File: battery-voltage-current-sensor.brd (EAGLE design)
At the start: 100 x 100 mm, 66 parts, among them IC1 ACS758LCB-050B-PFF-T, IC3 ADS1115IDGST, T1 C8545, T2 C8545, T3 C8545, X1 MKDSN1,5/2-5,08

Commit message: ready to manufacture, ordered
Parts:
- moved H1 0.60 mm to (17.4, 6.00)
- moved H2 0.60 mm to (17.4, 94.0)
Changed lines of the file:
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@@
 <layer number="25" name="tNames" color="7" fill="1" visible="yes" active="yes"/>
 <layer number="26" name="bNames" color="7" fill="1" visible="yes" active="yes"/>
-<layer number="27" name="tValues" color="7" fill="1" visible="no" active="yes"/>
-<layer number="28" name="bValues" color="7" fill="1" visible="no" active="yes"/>
+<layer number="27" name="tValues" color="7" fill="1" visible="yes" active="yes"/>
+<layer number="28" name="bValues" color="7" fill="1" visible="yes" active="yes"/>
 <layer number="29" name="tStop" color="7" fill="3" visible="no" active="yes"/>
 <layer number="30" name="bStop" color="7" fill="6" visible="no" active="yes"/>
@@
 <layer number="42" name="bRestrict" color="1" fill="10" visible="yes" active="yes"/>
 <layer number="43" name="vRestrict" color="2" fill="10" visible="no" active="yes"/>
-<layer number="44" name="Drills" color="7" fill="1" visible="no" active="yes"/>
-<layer number="45" name="Holes" color="7" fill="1" visible="no" active="yes"/>
+<layer number="44" name="Drills" color="7" fill="1" visible="yes" active="yes"/>
+<layer number="45" name="Holes" color="7" fill="1" visible="yes" active="yes"/>
 <layer number="46" name="Milling" color="3" fill="1" visible="no" active="yes"/>
 <layer number="47" name="Measures" color="7" fill="1" visible="no" active="yes"/>
@@
 <attribute name="VALUE" x="36.935" y="38.49" size="1.27" layer="27" align="center"/>
 </element>
-<element name="H1" library="holes" library_urn="urn:adsk.eagle:library:237" package="5,5-PAD-SQUARE" package3d_urn="urn:adsk.eagle:package:14299/1" value="MOUNT-PAD-SQUARE5.5" x="17.4" y="6.6" smashed="yes">
-<attribute name="POPULARITY" value="0" x="17.4" y="6.6" size="1.778" layer="27" display="off"/>
-</element>
-<element name="H2" library="holes" library_urn="urn:adsk.eagle:library:237" package="5,5-PAD-SQUARE" package3d_urn="urn:adsk.eagle:package:14299/1" value="MOUNT-PAD-SQUARE5.5" x="17.4" y="93.4" smashed="yes">
-<attribute name="POPULARITY" value="0" x="17.4" y="93.4" size="1.778" layer="27" display="off"/>
+<element name="H1" library="holes" library_urn="urn:adsk.eagle:library:237" package="5,5-PAD-SQUARE" package3d_urn="urn:adsk.eagle:package:14299/1" value="MOUNT-PAD-SQUARE5.5" x="17.4" y="6" smashed="yes">
+<attribute name="POPULARITY" value="0" x="17.4" y="6" size="1.778" layer="27" display="off"/>
+</element>
+<element name="H2" library="holes" library_urn="urn:adsk.eagle:library:237" package="5,5-PAD-SQUARE" package3d_urn="urn:adsk.eagle:package:14299/1" value="MOUNT-PAD-SQUARE5.5" x="17.4" y="94" smashed="yes">
+<attribute name="POPULARITY" value="0" x="17.4" y="94" size="1.778" layer="27" display="off"/>
 </element>
 <element name="H3" library="holes" library_urn="urn:adsk.eagle:library:237" package="5,5-PAD-SQUARE" package3d_urn="urn:adsk.eagle:package:14299/1" value="MOUNT-PAD-SQUARE5.5" x="50" y="94" smashed="yes">
@@
 <contactref element="R12" pad="1"/>
 <polygon width="0" layer="1" thermals="no">
-<vertex x="66" y="100.5"/>
+<vertex x="66.6" y="100.5"/>
 <vertex x="100.4" y="100.5"/>
-<vertex x="100.4" y="-1.1"/>
-<vertex x="66" y="-1.1"/>
+<vertex x="100.4" y="-1"/>
+<vertex x="66.6" y="-1"/>
 </polygon>
 <polygon width="0" layer="16" thermals="no">
-<vertex x="66" y="100.1"/>
+<vertex x="66.6" y="100.1"/>
 <vertex x="100.1" y="100.1"/>
 <vertex x="100.1" y="-0.1"/>
-<vertex x="66" y="-0.1"/>
+<vertex x="66.6" y="-0.1"/>
 </polygon>
 <wire x1="44.45" y1="65.2" x2="45.65" y2="64" width="0.254" layer="1"/>

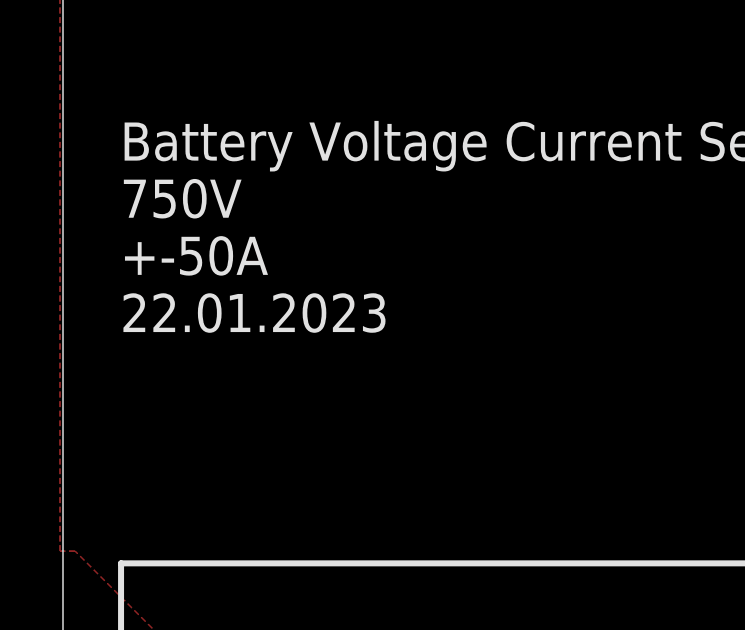
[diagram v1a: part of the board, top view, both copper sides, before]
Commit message: voltage measurement resistors changed to 100k
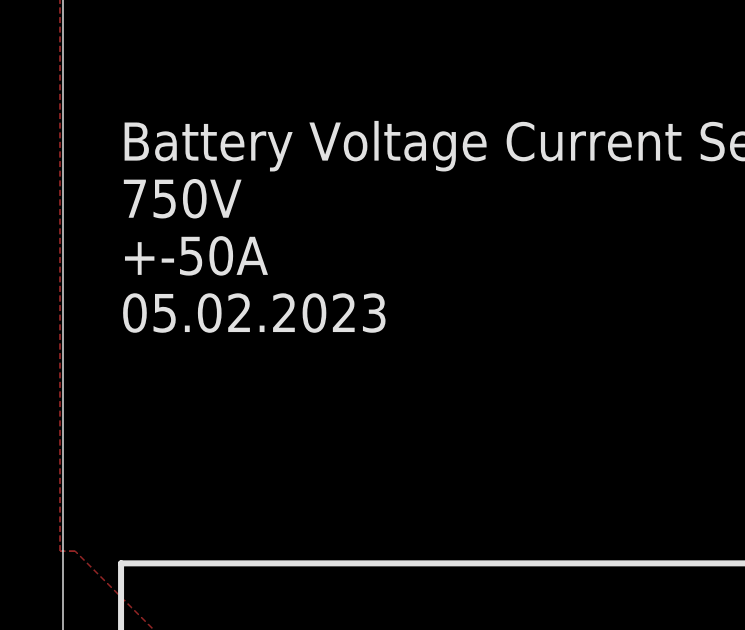
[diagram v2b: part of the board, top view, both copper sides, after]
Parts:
- R15, R16, R17, R18, R19, R20, R21, R22, R23, R4: value C17902 -> C17900
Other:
- board text added: "Battery Voltage Current Sensor 750V +-50A 05.02.2023"
- board text removed: "Battery Voltage Current Sensor 750V +-50A 22.01.2023"
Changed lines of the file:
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@@
 750V
 +-50A
-22.01.2023</text>
+05.02.2023</text>
 <text x="31.6" y="97" size="1.778" layer="25">Battery</text>
 <text x="30.4" y="2.8" size="1.778" layer="25">Output</text>
@@
 <attribute name="VALUE" x="81.6" y="91.2" size="1.27" layer="27" align="center"/>
 </element>
-<element name="R4" library="rcl" library_urn="urn:adsk.eagle:library:334" package="R1206" package3d_urn="urn:adsk.eagle:package:23540/2" value="C17902" x="44.4" y="67.7" smashed="yes" rot="R180"/>
-<element name="R15" library="rcl" library_urn="urn:adsk.eagle:library:334" package="R1206" package3d_urn="urn:adsk.eagle:package:23540/2" value="C17902" x="40.8" y="69.2" smashed="yes" rot="R90"/>
-<element name="R16" library="rcl" library_urn="urn:adsk.eagle:library:334" package="R1206" package3d_urn="urn:adsk.eagle:package:23540/2" value="C17902" x="39.3" y="72.8" smashed="yes" rot="R180"/>
-<element name="R17" library="rcl" library_urn="urn:adsk.eagle:library:334" package="R1206" package3d_urn="urn:adsk.eagle:package:23540/2" value="C17902" x="35.7" y="74.3" smashed="yes" rot="R90"/>
-<element name="R18" library="rcl" library_urn="urn:adsk.eagle:library:334" package="R1206" package3d_urn="urn:adsk.eagle:package:23540/2" value="C17902" x="35.7" y="79.4" smashed="yes" rot="R90"/>
-<element name="R19" library="rcl" library_urn="urn:adsk.eagle:library:334" package="R1206" package3d_urn="urn:adsk.eagle:package:23540/2" value="C17902" x="35.7" y="84.5" smashed="yes" rot="R90"/>
-<element name="R20" library="rcl" library_urn="urn:adsk.eagle:library:334" package="R1206" package3d_urn="urn:adsk.eagle:package:23540/2" value="C17902" x="35.7" y="89.6" smashed="yes" rot="R90"/>
-<element name="R21" library="rcl" library_urn="urn:adsk.eagle:library:334" package="R1206" package3d_urn="urn:adsk.eagle:package:23540/2" value="C17902" x="34.2" y="93.2" smashed="yes" rot="R180"/>
-<element name="R22" library="rcl" library_urn="urn:adsk.eagle:library:334" package="R1206" package3d_urn="urn:adsk.eagle:package:23540/2" value="C17902" x="31.4" y="95.3" smashed="yes" rot="R180"/>
-<element name="R23" library="rcl" library_urn="urn:adsk.eagle:library:334" package="R1206" package3d_urn="urn:adsk.eagle:package:23540/2" value="C17902" x="28.5" y="97.5" smashed="yes" rot="R180"/>
+<element name="R4" library="rcl" library_urn="urn:adsk.eagle:library:334" package="R1206" package3d_urn="urn:adsk.eagle:package:23540/2" value="C17900" x="44.4" y="67.7" smashed="yes" rot="R180"/>
+<element name="R15" library="rcl" library_urn="urn:adsk.eagle:library:334" package="R1206" package3d_urn="urn:adsk.eagle:package:23540/2" value="C17900" x="40.8" y="69.2" smashed="yes" rot="R90"/>
+<element name="R16" library="rcl" library_urn="urn:adsk.eagle:library:334" package="R1206" package3d_urn="urn:adsk.eagle:package:23540/2" value="C17900" x="39.3" y="72.8" smashed="yes" rot="R180"/>
+<element name="R17" library="rcl" library_urn="urn:adsk.eagle:library:334" package="R1206" package3d_urn="urn:adsk.eagle:package:23540/2" value="C17900" x="35.7" y="74.3" smashed="yes" rot="R90"/>
+<element name="R18" library="rcl" library_urn="urn:adsk.eagle:library:334" package="R1206" package3d_urn="urn:adsk.eagle:package:23540/2" value="C17900" x="35.7" y="79.4" smashed="yes" rot="R90"/>
+<element name="R19" library="rcl" library_urn="urn:adsk.eagle:library:334" package="R1206" package3d_urn="urn:adsk.eagle:package:23540/2" value="C17900" x="35.7" y="84.5" smashed="yes" rot="R90"/>
+<element name="R20" library="rcl" library_urn="urn:adsk.eagle:library:334" package="R1206" package3d_urn="urn:adsk.eagle:package:23540/2" value="C17900" x="35.7" y="89.6" smashed="yes" rot="R90"/>
+<element name="R21" library="rcl" library_urn="urn:adsk.eagle:library:334" package="R1206" package3d_urn="urn:adsk.eagle:package:23540/2" value="C17900" x="34.2" y="93.2" smashed="yes" rot="R180"/>
+<element name="R22" library="rcl" library_urn="urn:adsk.eagle:library:334" package="R1206" package3d_urn="urn:adsk.eagle:package:23540/2" value="C17900" x="31.4" y="95.3" smashed="yes" rot="R180"/>
+<element name="R23" library="rcl" library_urn="urn:adsk.eagle:library:334" package="R1206" package3d_urn="urn:adsk.eagle:package:23540/2" value="C17900" x="28.5" y="97.5" smashed="yes" rot="R180"/>
 <element name="R24" library="rcl" library_urn="urn:adsk.eagle:library:334" package="R0805" package3d_urn="urn:adsk.eagle:package:23553/2" value="C17772" x="45.9" y="71.15" smashed="yes" rot="R270"/>
 <element name="C4" library="rcl" library_urn="urn:adsk.eagle:library:334" package="C0805" package3d_urn="urn:adsk.eagle:package:23617/2" value="100nF" x="76.5" y="92.3" smashed="yes" rot="R180">

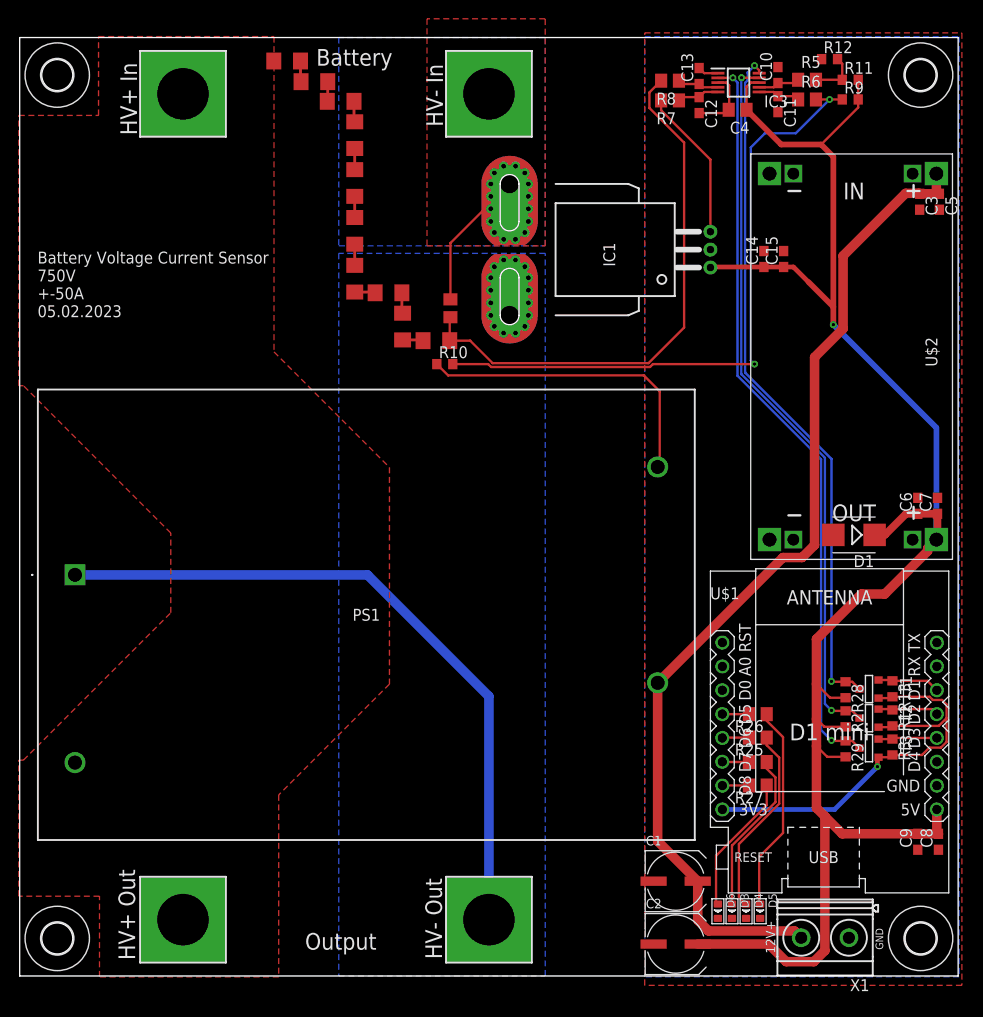
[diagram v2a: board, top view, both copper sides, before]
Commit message: 1000V DCDC position corrected
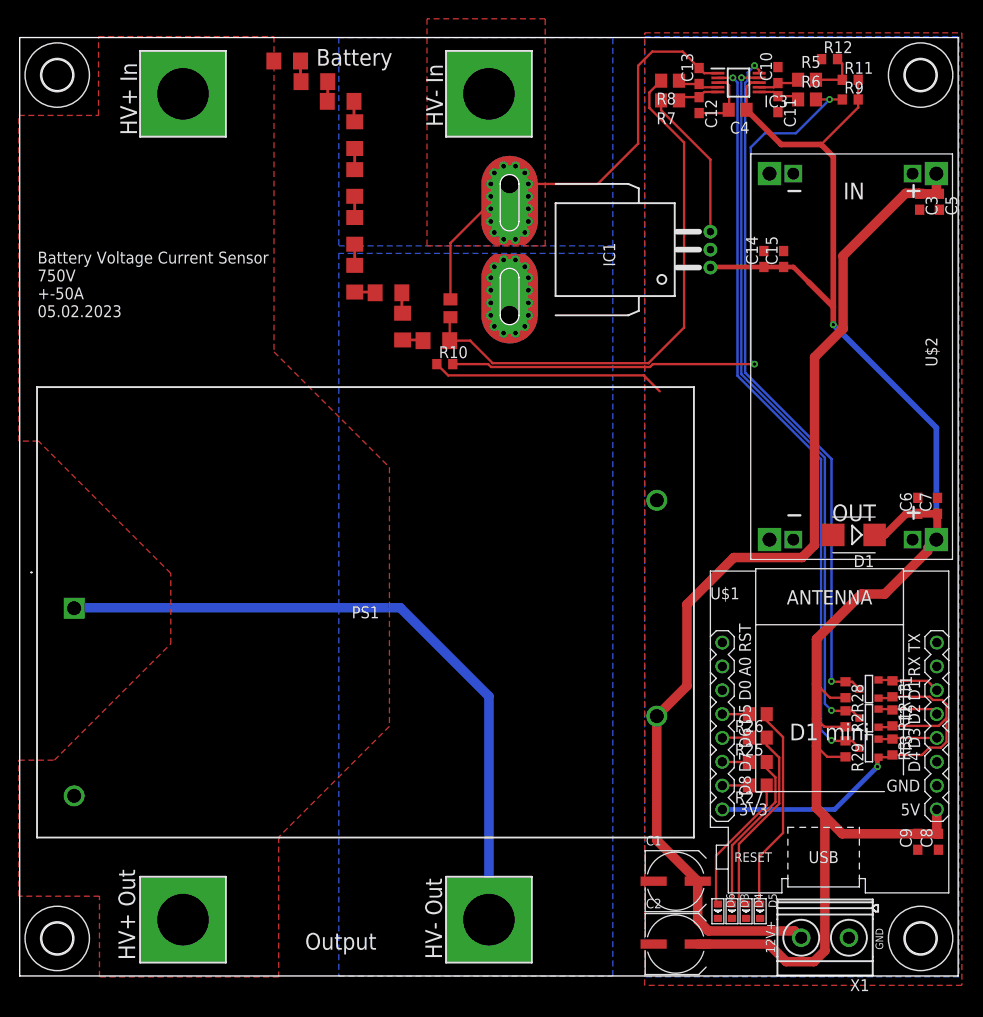
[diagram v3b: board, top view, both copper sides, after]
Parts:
- moved PS1 0.28 mm to (5.80, 43.0)
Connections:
- removed net HV-IN: H3.B5,5, IC1.IP+, IC1.IP+@10, IC1.IP+@11, IC1.IP+@12, IC1.IP+@13, IC1.IP+@14, IC1.IP+@15, IC1.IP+@16, IC1.IP+@17, IC1.IP+@2, IC1.IP+@3, IC1.IP+@4, IC1.IP+@5, IC1.IP+@6, IC1.IP+@7, IC1.IP+@8, IC1.IP+@9, R24.1
- net GND: now also H3.B5,5, IC1.IP+, IC1.IP+@10, IC1.IP+@11, IC1.IP+@12, IC1.IP+@13, IC1.IP+@14, IC1.IP+@15, IC1.IP+@16, IC1.IP+@17, IC1.IP+@2, IC1.IP+@3, IC1.IP+@4, IC1.IP+@5, IC1.IP+@6, IC1.IP+@7, IC1.IP+@8, IC1.IP+@9, R24.1
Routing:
- net GND: track 42.6 -> 81.0 mm
- net HV-IN: track 14.9 -> 0.00 mm
- net +12V/1: track 109.1 -> 112.2 mm
- net HV-: track 73.3 -> 71.9 mm
- removed copper zone on layer 1, net HV-IN
- removed copper zone on layer 16, net HV-IN

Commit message: error fixed
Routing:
- net GND: track 81.0 -> 92.7 mm
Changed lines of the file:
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@@
 <vertex x="56" y="102"/>
 </polygon>
+<wire x1="68.2" y1="62.3" x2="68.2" y2="51" width="0.1524" layer="1"/>
+<wire x1="68.2" y1="51" x2="67.89" y2="50.69" width="0.1524" layer="1"/>
 </signal>
 <signal name="+5V/1">

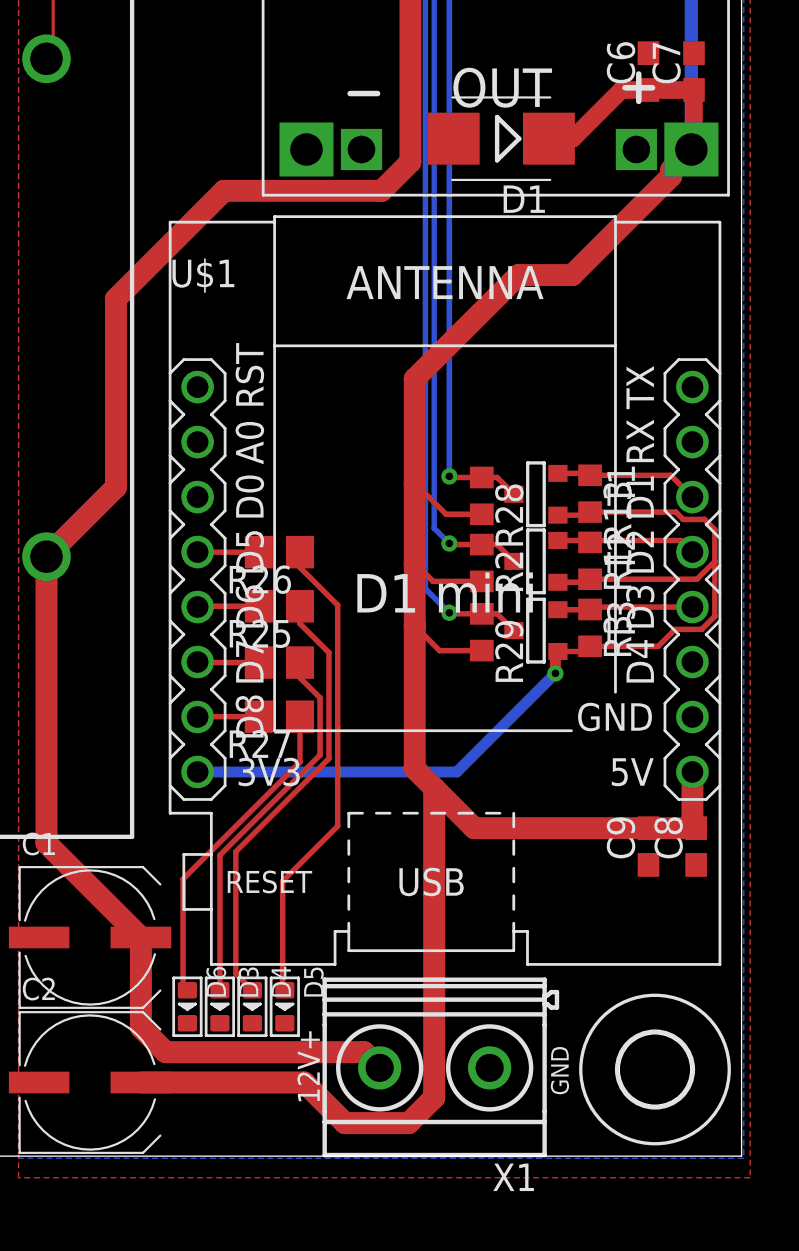
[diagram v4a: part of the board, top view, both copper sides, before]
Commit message: connector swapped against a 4pin for a display
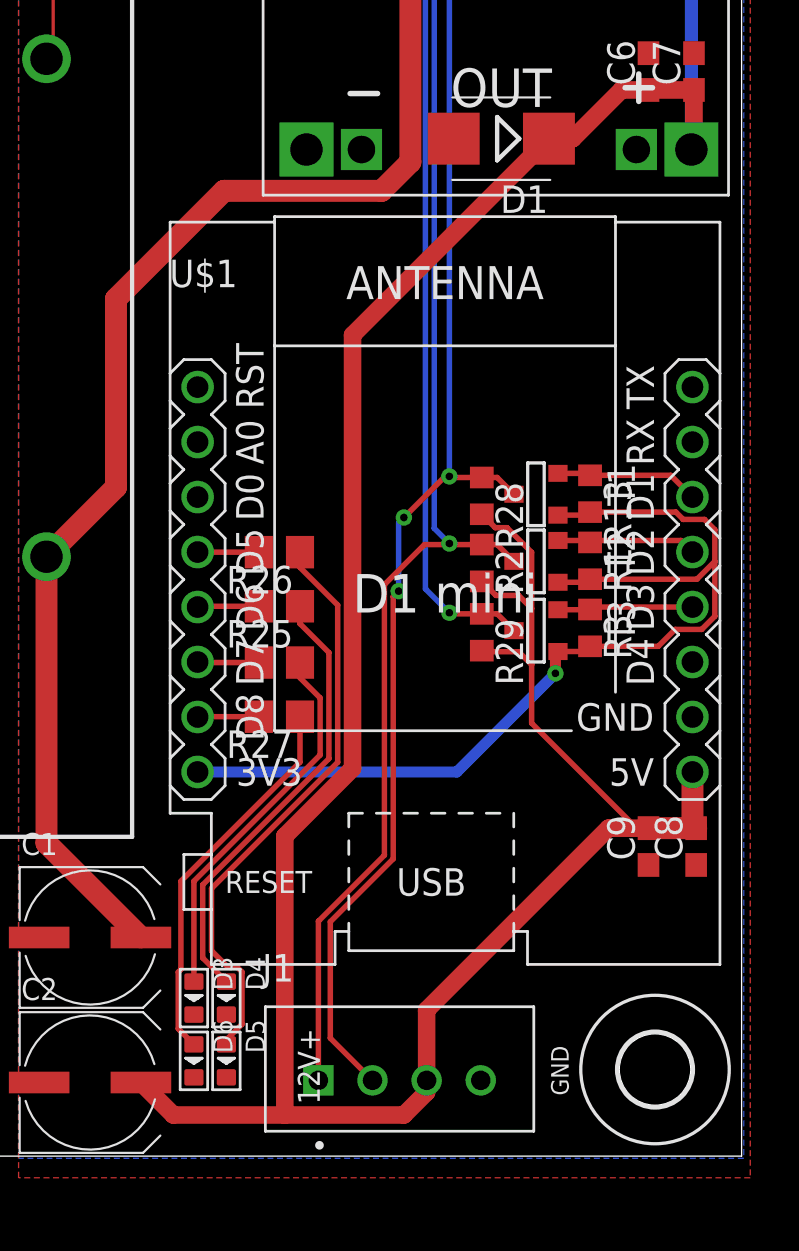
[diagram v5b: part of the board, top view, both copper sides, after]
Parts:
- removed X1: MKDSN1,5/2-5,08, con-phoenix-508:MKDSN1,5/2-5,08
- added J1: B4B-XH-A(LF)(SN), Headers:B4B-XH-A(LF)(SN)
- moved D5 3.68 mm to (76.2, 4.40)
- moved D6 2.52 mm to (74.7, 4.40)
- moved D3 1.26 mm to (74.7, 7.30)
- moved D4 1.26 mm to (76.2, 7.30)
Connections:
- net +12V/1: no longer X1.2
- net +5V/1: now also J1.3
- net GND: now also J1.4; no longer X1.1
- net SCL: now also J1.2
- net SDA: now also J1.1
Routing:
- net SCL: track 74.2 -> 105.3 mm, vias 2 -> 4
- net SDA: track 76.6 -> 104.6 mm
- net +5V/1: track 186.5 -> 205.0 mm
- net +12V/1: track 112.2 -> 96.3 mm
- net N$7: track 22.1 -> 27.0 mm
- net N$17: track 15.0 -> 17.8 mm
